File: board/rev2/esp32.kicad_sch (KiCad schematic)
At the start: 2 parts, among them J3 Conn_01x06_Pin, U6 ESP32-C6-WROOM-1

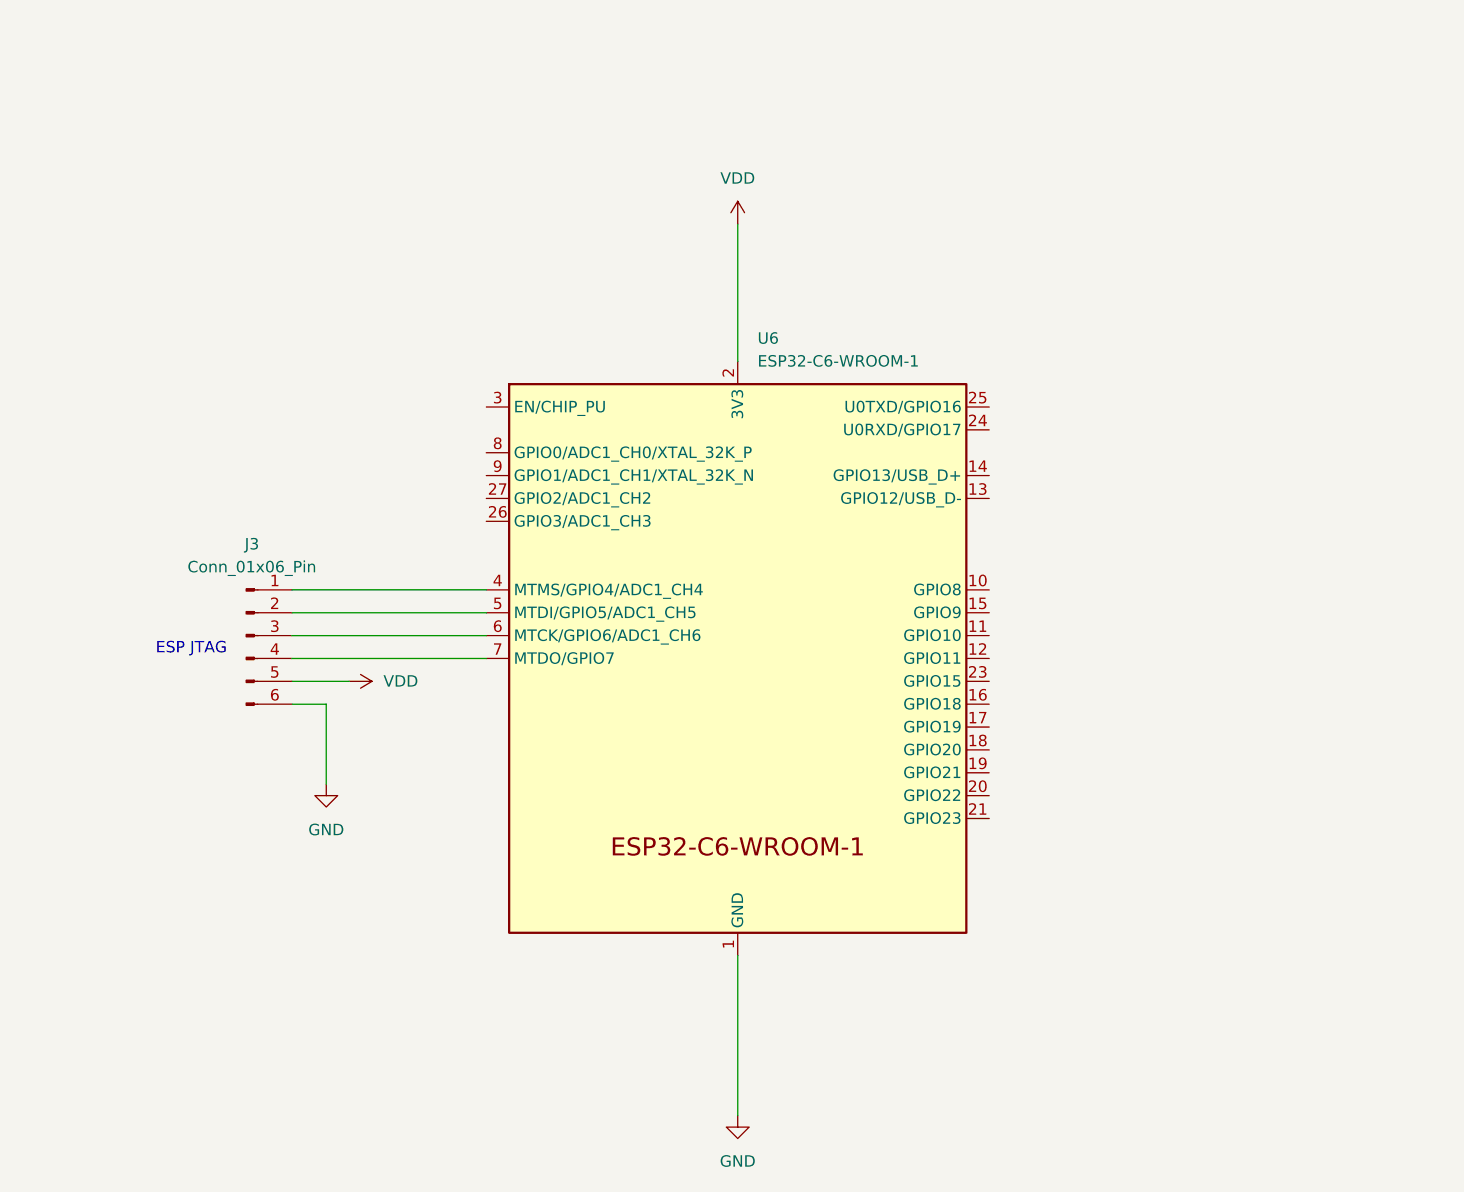
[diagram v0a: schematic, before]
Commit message: Board GPIO allocation
- and usbmux

still need to do termination on the big buses + a bunch of bypass caps
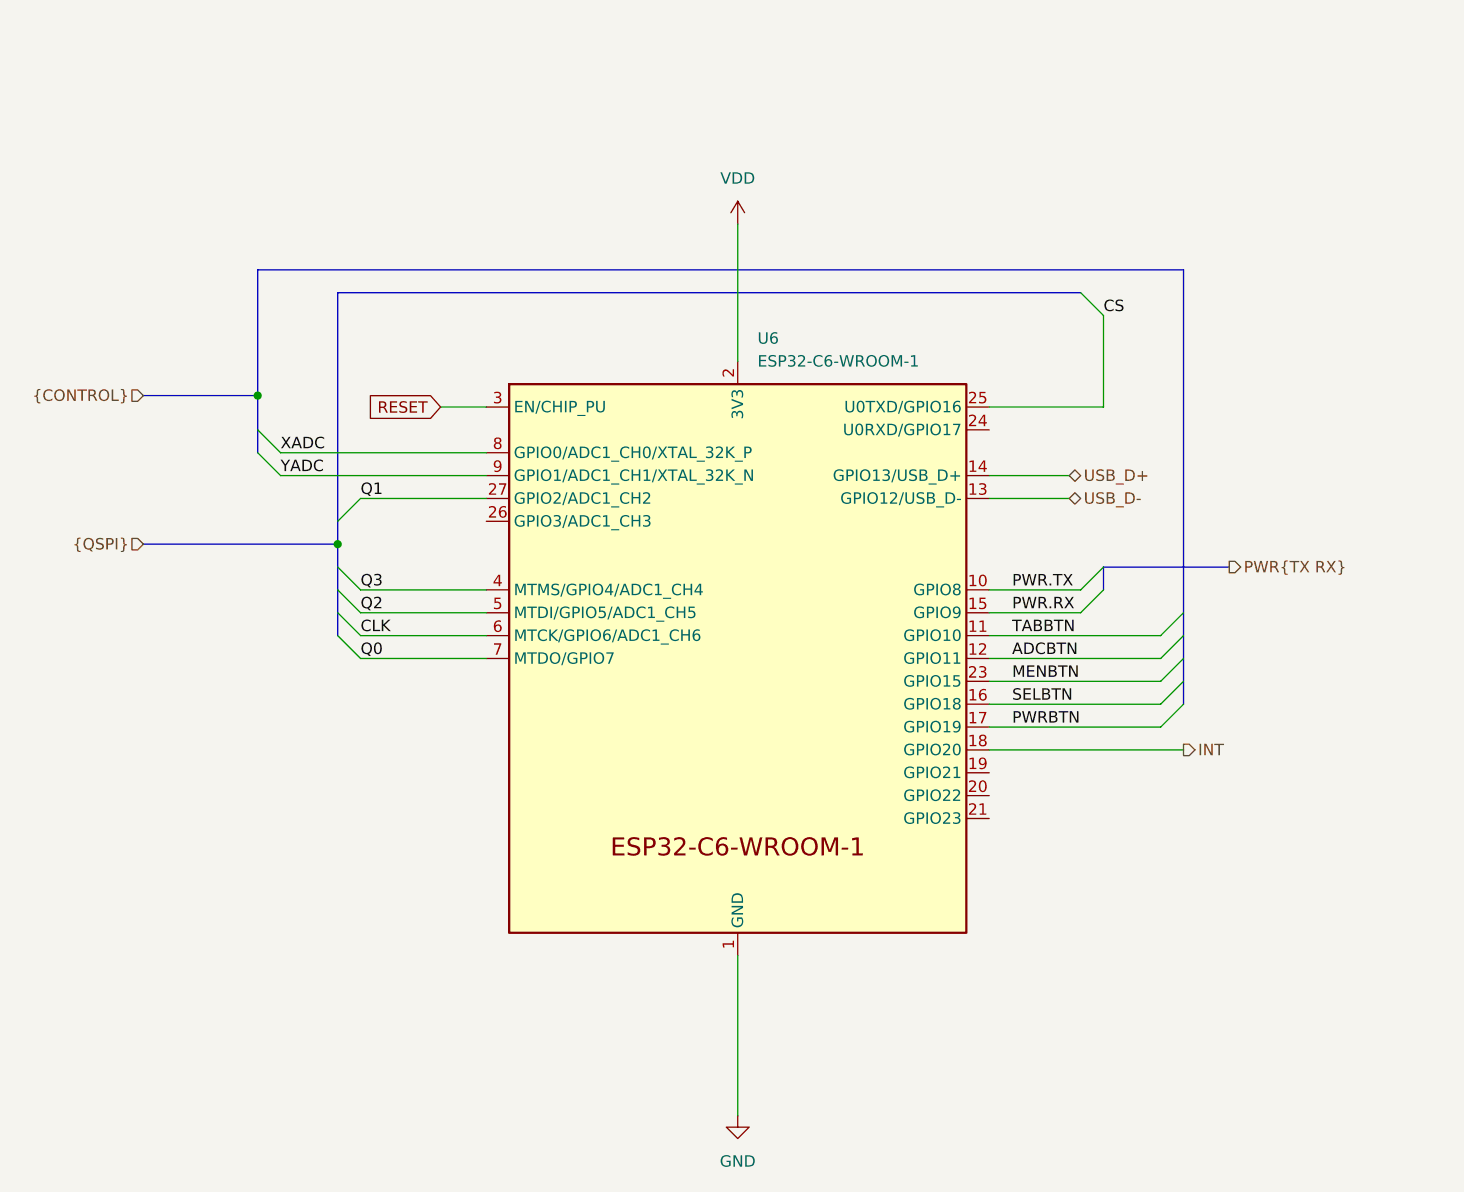
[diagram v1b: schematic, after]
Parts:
- removed J3: Conn_01x06_Pin, symbol Connector:Conn_01x06_Pin
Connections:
- net Q3: now reaches U6.4 (MTMS/GPIO4/ADC1_CH4)
- net Q2: now reaches U6.5 (MTDI/GPIO5/ADC1_CH5)
- net CLK: now reaches U6.6 (MTCK/GPIO6/ADC1_CH6)
- net Q0: now reaches U6.7 (MTDO/GPIO7)
- net PWR.TX: now reaches U6.10 (GPIO8)
- net TABBTN: now reaches U6.11 (GPIO10)
- net ADCBTN: now reaches U6.12 (GPIO11)
- net USB_D-: now reaches U6.13 (GPIO12/USB_D-)
- net USB_D+: now reaches U6.14 (GPIO13/USB_D+)
- net PWR.RX: now reaches U6.15 (GPIO9)
- net SELBTN: now reaches U6.16 (GPIO18)
- net PWRBTN: now reaches U6.17 (GPIO19)
- net INT: now reaches U6.18 (GPIO20)
- net MENBTN: now reaches U6.23 (GPIO15)
- net CS: now reaches U6.25 (U0TXD/GPIO16)
- net Q1: now reaches U6.27 (GPIO2/ADC1_CH2)
- net RESET: now reaches U6.3 (EN/CHIP_PU)
- net XADC: now reaches U6.8 (GPIO0/ADC1_CH0/XTAL_32K_P)
- net YADC: now reaches U6.9 (GPIO1/ADC1_CH1/XTAL_32K_N)
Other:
- note removed: "ESP JTAG"
- company: (none) -> MLABS
- title: (none) -> WiFi Microcontroller

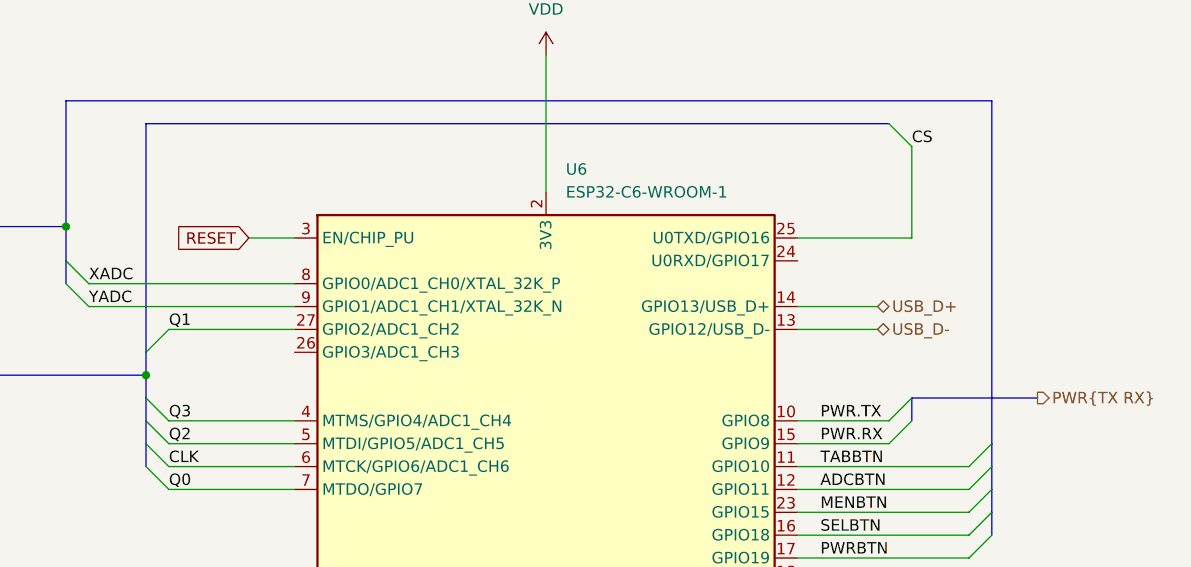
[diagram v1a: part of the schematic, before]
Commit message: Continue board, assign caps/res, adjust for JLC availability
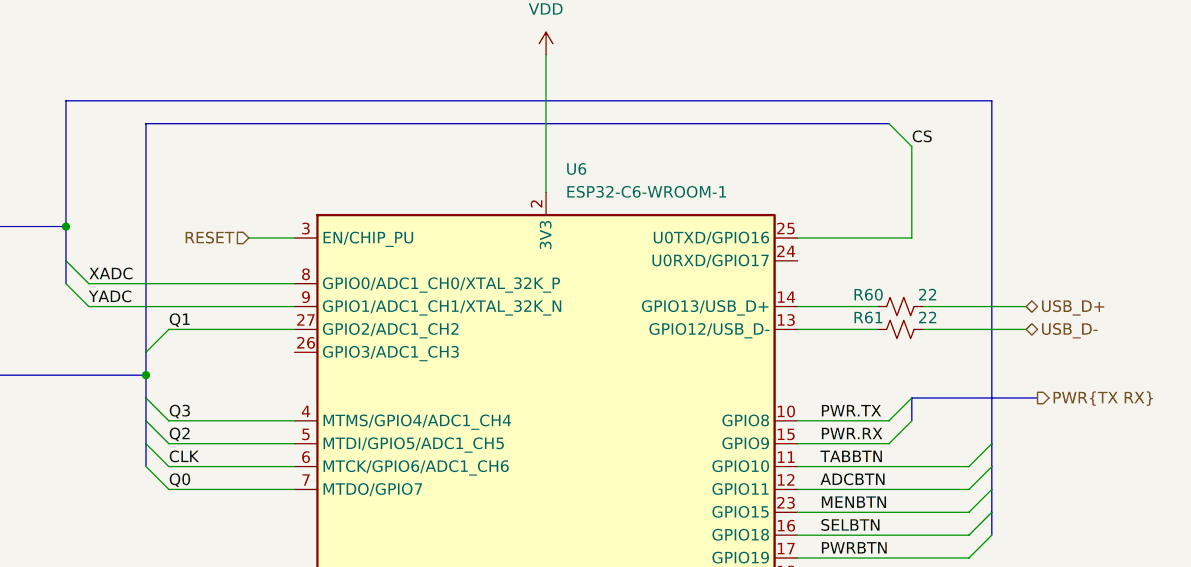
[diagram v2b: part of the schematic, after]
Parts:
- added R60, R61: 22, Resistor_SMD:R_0402_1005Metric, symbol Device:R_Small_US
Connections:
- net USB_D+: now also R60.2; no longer U6.14 (GPIO13/USB_D+)
- net USB_D-: now also R61.2; no longer U6.13 (GPIO12/USB_D-)
- new net: R61.1, U6.13 (GPIO12/USB_D-)
- new net: R60.1, U6.14 (GPIO13/USB_D+)

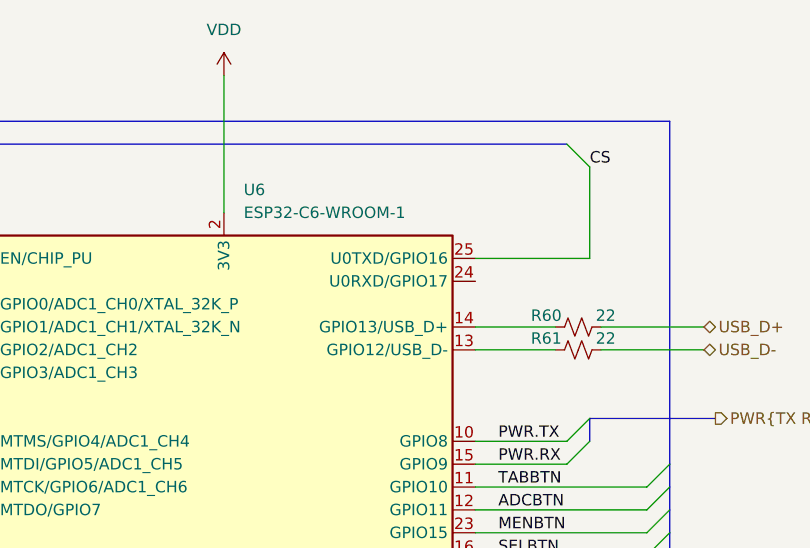
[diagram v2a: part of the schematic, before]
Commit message: Start new PCB
- all footprints setup
- need to setup netclasses next, tho
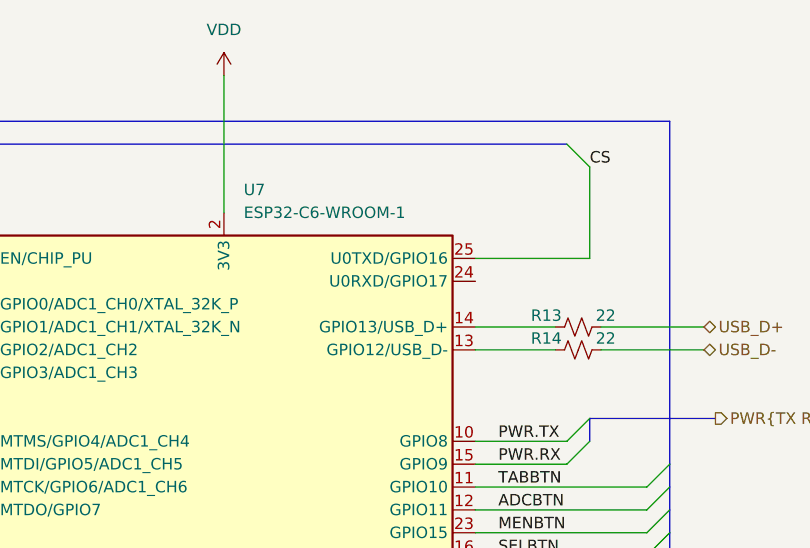
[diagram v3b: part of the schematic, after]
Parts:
- U7: renamed from U6; Part (none) -> ESP32-C6-WROOM-1
- renumbered R60 to R13, R61 to R14
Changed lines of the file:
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@@
 		(dnp no)
 		(fields_autoplaced yes)
-		(property "Reference" "#PWR015"
+		(property "Reference" "#PWR018"
 			(at 138.43 48.26 0)
 			(effects
@@
 			(project "mainboard"
 				(path "/32eb05c7-b4a6-42f3-8fb3-43453631100f/ab8e590b-cde3-4860-87b4-37e60f787bc4"
-					(reference "#PWR015")
+					(reference "#PWR018")
 					(unit 1)
 				)
@@
 		(on_board yes)
 		(dnp no)
-		(property "Reference" "R61"
+		(property "Reference" "R14"
 			(at 174.244 73.66 90)
 			(effects
@@
 			(project "mainboard"
 				(path "/32eb05c7-b4a6-42f3-8fb3-43453631100f/ab8e590b-cde3-4860-87b4-37e60f787bc4"
-					(reference "R61")
+					(reference "R14")
 					(unit 1)
 				)
@@
 		(on_board yes)
 		(dnp no)
-		(property "Reference" "R60"
+		(property "Reference" "R13"
 			(at 174.244 71.12 90)
 			(effects
@@
 			(project "mainboard"
 				(path "/32eb05c7-b4a6-42f3-8fb3-43453631100f/ab8e590b-cde3-4860-87b4-37e60f787bc4"
-					(reference "R60")
+					(reference "R13")
 					(unit 1)
 				)
@@
 		(dnp no)
 		(fields_autoplaced yes)
-		(property "Reference" "#PWR016"
+		(property "Reference" "#PWR019"
 			(at 138.43 149.86 0)
 			(effects
@@
 			(project "mainboard"
 				(path "/32eb05c7-b4a6-42f3-8fb3-43453631100f/ab8e590b-cde3-4860-87b4-37e60f787bc4"
-					(reference "#PWR016")
+					(reference "#PWR019")
 					(unit 1)
 				)
@@
 		(dnp no)
 		(fields_autoplaced yes)
-		(property "Reference" "U6"
+		(property "Reference" "U7"
 			(at 140.6241 57.15 0)
 			(effects
@@
 					(size 1.27 1.27)
 					(color 255 255 194 1)
+				)
+				(hide yes)
+			)
+		)
+		(property "Part" "ESP32-C6-WROOM-1"
+			(at 138.43 92.71 0)
+			(effects
+				(font
+					(size 1.27 1.27)
 				)
 				(hide yes)
@@
 			(project "mainboard"
 				(path "/32eb05c7-b4a6-42f3-8fb3-43453631100f/ab8e590b-cde3-4860-87b4-37e60f787bc4"
-					(reference "U6")
+					(reference "U7")
 					(unit 1)
 				)
